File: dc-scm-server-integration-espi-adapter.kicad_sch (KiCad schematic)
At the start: 12 parts

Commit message: [#103753] Update symbol libraries
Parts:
- FD1001, FD1002, FD1003, FD1004, FD1007, FD1008: symbol Antmicro Symbols:Fiducial_1mm_Mask2mm -> antmicroFiducialMarks:Fiducial_1mm_Mask2mm
- H1001, H1002, H1003, H1004: symbol MechanicalParts:Spacer_Drill4.4mm_H6mm_9774060360R -> antmicroMechanicalParts:Spacer_Drill4.4mm_H6mm_9774060360R
- N1001: symbol Antmicro Symbols:antmicro_logo -> antmicroMechanicalParts:antmicro_logo
- N1002: symbol Antmicro Symbols:oshw_logo -> antmicroMechanicalParts:oshw_logo
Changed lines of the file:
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@@
 	)
 	(symbol
-		(lib_id "MechanicalParts:Spacer_Drill4.4mm_H6mm_9774060360R")
+		(lib_id "antmicroMechanicalParts:Spacer_Drill4.4mm_H6mm_9774060360R")
 		(at 224.79 134.62 0)
 		(unit 1)
@@
 	)
 	(symbol
-		(lib_id "Antmicro Symbols:Fiducial_1mm_Mask2mm")
+		(lib_id "antmicroFiducialMarks:Fiducial_1mm_Mask2mm")
 		(at 255.27 165.1 0)
 		(unit 1)
@@
 	)
 	(symbol
-		(lib_id "Antmicro Symbols:antmicro_logo")
+		(lib_id "antmicroMechanicalParts:antmicro_logo")
 		(at 224.79 166.37 0)
 		(unit 1)
@@
 	)
 	(symbol
-		(lib_id "MechanicalParts:Spacer_Drill4.4mm_H6mm_9774060360R")
+		(lib_id "antmicroMechanicalParts:Spacer_Drill4.4mm_H6mm_9774060360R")
 		(at 224.79 149.86 0)
 		(unit 1)
@@
 	)
 	(symbol
-		(lib_id "MechanicalParts:Spacer_Drill4.4mm_H6mm_9774060360R")
+		(lib_id "antmicroMechanicalParts:Spacer_Drill4.4mm_H6mm_9774060360R")
 		(at 224.79 142.24 0)
 		(unit 1)
@@
 	)
 	(symbol
-		(lib_id "Antmicro Symbols:oshw_logo")
+		(lib_id "antmicroMechanicalParts:oshw_logo")
 		(at 224.79 173.99 0)
 		(unit 1)
@@
 	)
 	(symbol
-		(lib_id "Antmicro Symbols:Fiducial_1mm_Mask2mm")
+		(lib_id "antmicroFiducialMarks:Fiducial_1mm_Mask2mm")
 		(at 255.27 142.24 0)
 		(unit 1)
@@
 	)
 	(symbol
-		(lib_id "Antmicro Symbols:GND")
+		(lib_id "antmicropower:GND")
 		(at 222.25 152.4 0)
 		(unit 1)
@@
 		(dnp no)
 		(fields_autoplaced yes)
-		(property "Reference" "#PWR01001"
+		(property "Reference" "#PWR1001"
 			(at 231.14 154.94 0)
 			(hide yes)
@@
 			(project "dc-scm-server-integration-espi-adapter"
 				(path "/df391740-647e-4ab6-9dcd-d61184d66fe9"
-					(reference "#PWR01001")
+					(reference "#PWR1001")
 					(unit 1)
 				)
@@
 	)
 	(symbol
-		(lib_id "Antmicro Symbols:Fiducial_1mm_Mask2mm")
+		(lib_id "antmicroFiducialMarks:Fiducial_1mm_Mask2mm")
 		(at 255.27 134.62 0)
 		(unit 1)
@@
 	)
 	(symbol
-		(lib_id "Antmicro Symbols:Fiducial_1mm_Mask2mm")
+		(lib_id "antmicroFiducialMarks:Fiducial_1mm_Mask2mm")
 		(at 255.27 172.72 0)
 		(unit 1)
@@
 	)
 	(symbol
-		(lib_id "Antmicro Symbols:Fiducial_1mm_Mask2mm")
+		(lib_id "antmicroFiducialMarks:Fiducial_1mm_Mask2mm")
 		(at 255.27 149.86 0)
 		(unit 1)
@@
 	)
 	(symbol
-		(lib_id "MechanicalParts:Spacer_Drill4.4mm_H6mm_9774060360R")
+		(lib_id "antmicroMechanicalParts:Spacer_Drill4.4mm_H6mm_9774060360R")
 		(at 224.79 127 0)
 		(unit 1)
@@
 	)
 	(symbol
-		(lib_id "Antmicro Symbols:Fiducial_1mm_Mask2mm")
+		(lib_id "antmicroFiducialMarks:Fiducial_1mm_Mask2mm")
 		(at 255.27 157.48 0)
 		(unit 1)

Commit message: [#103697] Reenumerate the entire schematic, rerouting eSPI to maintain bigger gap between traces, rerouting the LDO
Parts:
- renumbered FD1001 to FD1, FD1002 to FD2, FD1003 to FD3, FD1004 to FD4, FD1007 to FD5, FD1008 to FD6, H1001 to H1, H1002 to H2, H1003 to H3, H1004 to H4, N1001 to N1, N1002 to N2
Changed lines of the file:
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@@
 		(dnp no)
 		(fields_autoplaced yes)
-		(property "Reference" "H1002"
+		(property "Reference" "H2"
 			(at 233.68 133.35 0)
 			(show_name no)
@@
 			(project "dc-scm-server-integration-espi-adapter"
 				(path "/df391740-647e-4ab6-9dcd-d61184d66fe9"
-					(reference "H1002")
+					(reference "H2")
 					(unit 1)
 				)
@@
 		(dnp no)
 		(fields_autoplaced yes)
-		(property "Reference" "FD1007"
+		(property "Reference" "FD5"
 			(at 259.08 163.83 0)
 			(show_name no)
@@
 			(project "dc-scm-server-integration-espi-adapter"
 				(path "/df391740-647e-4ab6-9dcd-d61184d66fe9"
-					(reference "FD1007")
+					(reference "FD5")
 					(unit 1)
 				)
@@
 		(dnp no)
 		(fields_autoplaced yes)
-		(property "Reference" "N1001"
+		(property "Reference" "N1"
 			(at 231.14 164.3862 0)
 			(show_name no)
@@
 			(project "dc-scm-server-integration-espi-adapter"
 				(path "/df391740-647e-4ab6-9dcd-d61184d66fe9"
-					(reference "N1001")
+					(reference "N1")
 					(unit 1)
 				)
@@
 		(dnp no)
 		(fields_autoplaced yes)
-		(property "Reference" "H1004"
+		(property "Reference" "H4"
 			(at 233.68 148.59 0)
 			(show_name no)
@@
 			(project "dc-scm-server-integration-espi-adapter"
 				(path "/df391740-647e-4ab6-9dcd-d61184d66fe9"
-					(reference "H1004")
+					(reference "H4")
 					(unit 1)
 				)
@@
 		(dnp no)
 		(fields_autoplaced yes)
-		(property "Reference" "H1003"
+		(property "Reference" "H3"
 			(at 233.68 140.97 0)
 			(show_name no)
@@
 			(project "dc-scm-server-integration-espi-adapter"
 				(path "/df391740-647e-4ab6-9dcd-d61184d66fe9"
-					(reference "H1003")
+					(reference "H3")
 					(unit 1)
 				)
@@
 		(dnp no)
 		(fields_autoplaced yes)
-		(property "Reference" "N1002"
+		(property "Reference" "N2"
 			(at 231.14 172.0062 0)
 			(show_name no)
@@
 			(project "dc-scm-server-integration-espi-adapter"
 				(path "/df391740-647e-4ab6-9dcd-d61184d66fe9"
-					(reference "N1002")
+					(reference "N2")
 					(unit 1)
 				)
@@
 		(dnp no)
 		(fields_autoplaced yes)
-		(property "Reference" "FD1002"
+		(property "Reference" "FD2"
 			(at 259.08 140.97 0)
 			(show_name no)
@@
 			(project "dc-scm-server-integration-espi-adapter"
 				(path "/df391740-647e-4ab6-9dcd-d61184d66fe9"
-					(reference "FD1002")
+					(reference "FD2")
 					(unit 1)
 				)
@@
 		(dnp no)
 		(fields_autoplaced yes)
-		(property "Reference" "#PWR1001"
+		(property "Reference" "#PWR01"
 			(at 231.14 154.94 0)
 			(hide yes)
@@
 			(project "dc-scm-server-integration-espi-adapter"
 				(path "/df391740-647e-4ab6-9dcd-d61184d66fe9"
-					(reference "#PWR1001")
+					(reference "#PWR01")
 					(unit 1)
 				)
@@
 		(dnp no)
 		(fields_autoplaced yes)
-		(property "Reference" "FD1001"
+		(property "Reference" "FD1"
 			(at 259.08 133.35 0)
 			(show_name no)
@@
 			(project "dc-scm-server-integration-espi-adapter"
 				(path "/df391740-647e-4ab6-9dcd-d61184d66fe9"
-					(reference "FD1001")
+					(reference "FD1")
 					(unit 1)
 				)
@@
 		(dnp no)
 		(fields_autoplaced yes)
-		(property "Reference" "FD1008"
+		(property "Reference" "FD6"
 			(at 259.08 171.45 0)
 			(show_name no)
@@
 			(project "dc-scm-server-integration-espi-adapter"
 				(path "/df391740-647e-4ab6-9dcd-d61184d66fe9"
-					(reference "FD1008")
+					(reference "FD6")
 					(unit 1)
 				)
@@
 		(dnp no)
 		(fields_autoplaced yes)
-		(property "Reference" "FD1003"
+		(property "Reference" "FD3"
 			(at 259.08 148.59 0)
 			(show_name no)
@@
 			(project "dc-scm-server-integration-espi-adapter"
 				(path "/df391740-647e-4ab6-9dcd-d61184d66fe9"
-					(reference "FD1003")
+					(reference "FD3")
 					(unit 1)
 				)
@@
 		(dnp no)
 		(fields_autoplaced yes)
-		(property "Reference" "H1001"
+		(property "Reference" "H1"
 			(at 233.68 125.73 0)
 			(show_name no)
@@
 			(project "dc-scm-server-integration-espi-adapter"
 				(path "/df391740-647e-4ab6-9dcd-d61184d66fe9"
-					(reference "H1001")
+					(reference "H1")
 					(unit 1)
 				)
@@
 		(dnp no)
 		(fields_autoplaced yes)
-		(property "Reference" "FD1004"
+		(property "Reference" "FD4"
 			(at 259.08 156.21 0)
 			(show_name no)
@@
 			(project "dc-scm-server-integration-espi-adapter"
 				(path "/df391740-647e-4ab6-9dcd-d61184d66fe9"
-					(reference "FD1004")
+					(reference "FD4")
 					(unit 1)
 				)

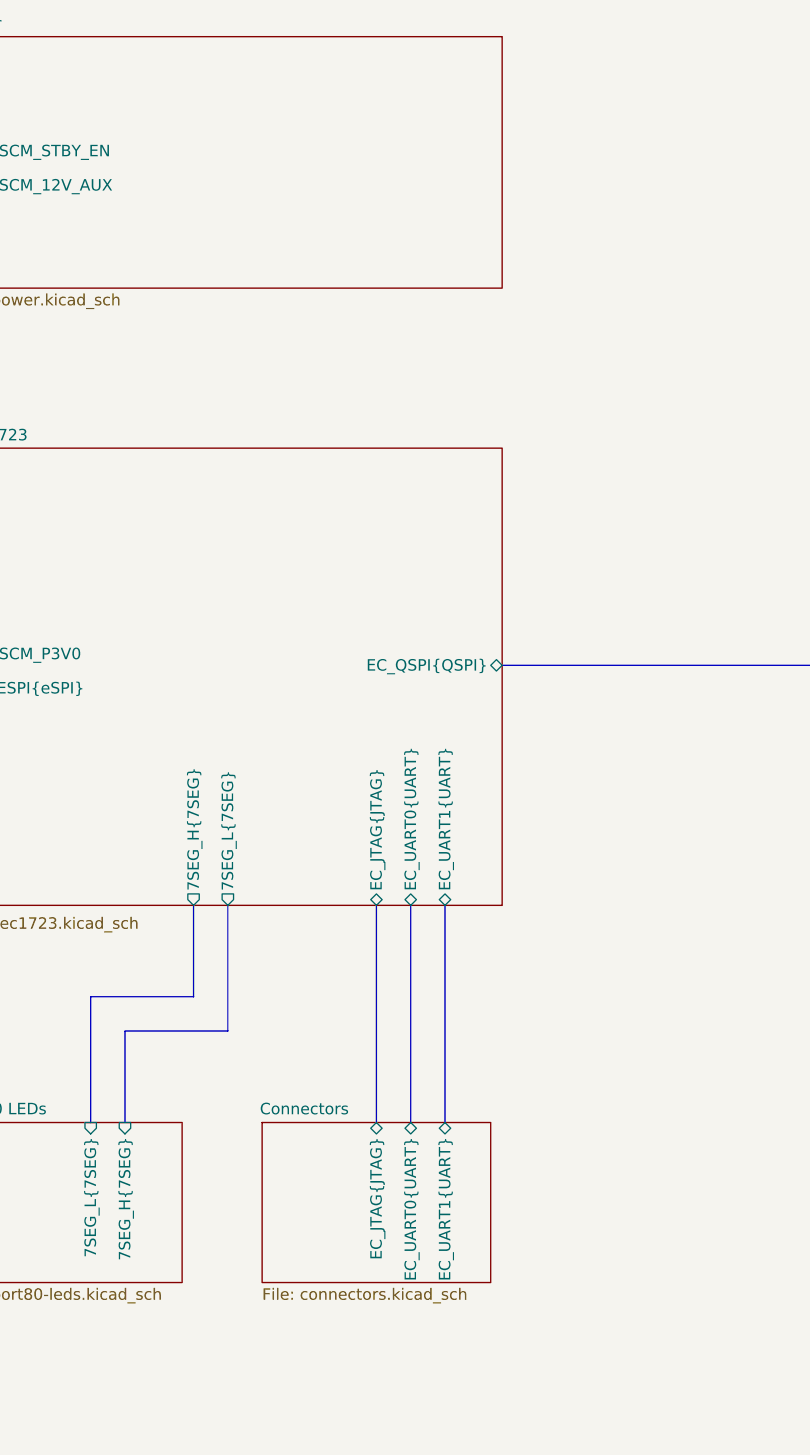
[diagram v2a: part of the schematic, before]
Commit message: [#103697] Change LDO layout, add power from USB, fix length tuning, change In4.Cu to GND/SIG and In5.Cu to 3V3, cleanup the design
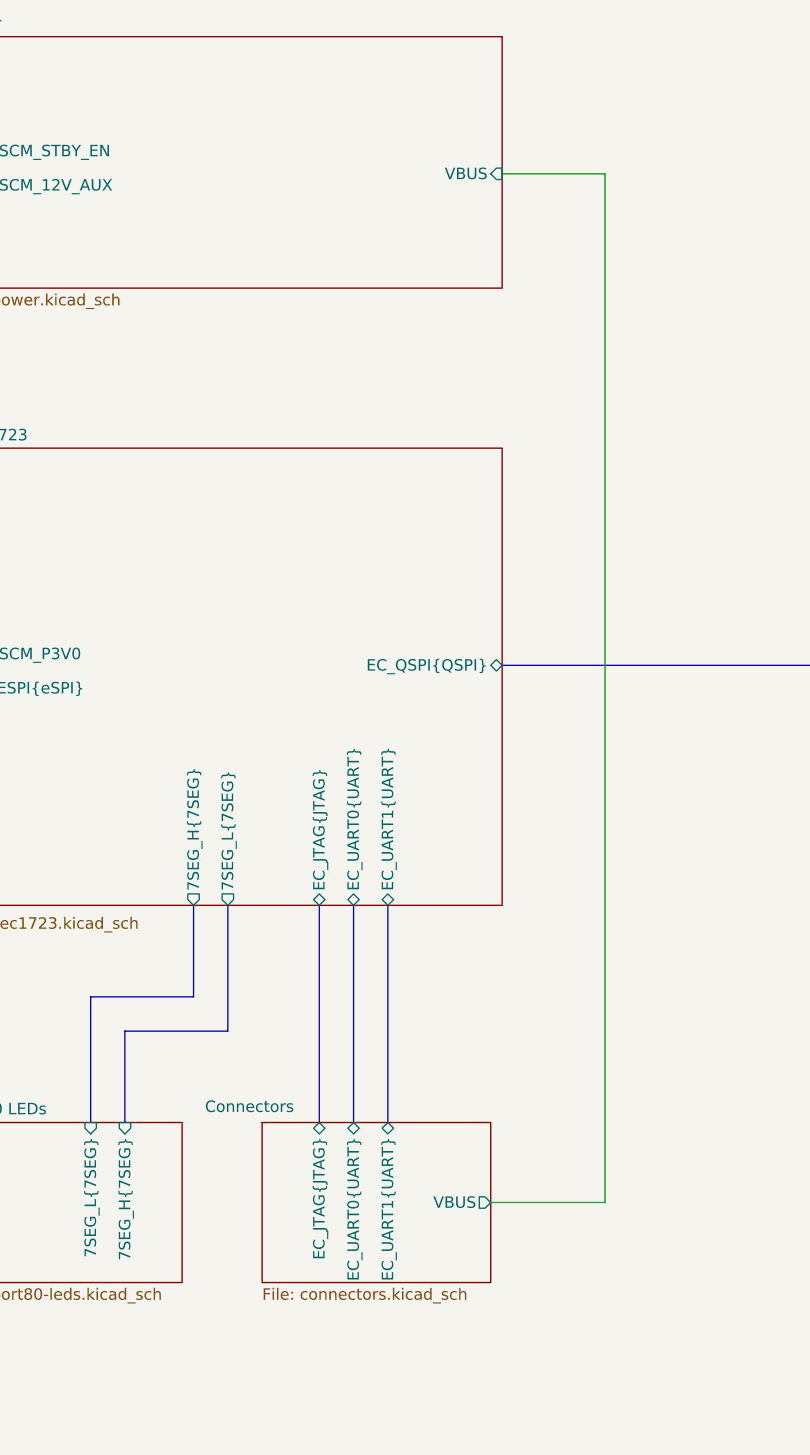
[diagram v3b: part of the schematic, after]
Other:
- sheet Connectors ports: added VBUS; removed none
- sheet Power ports: added VBUS; removed none
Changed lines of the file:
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@@
 		(color 0 0 0 0)
 	)
+	(wire
+		(pts
+			(xy 190.5 35.56) (xy 179.07 35.56)
+		)
+		(stroke
+			(width 0)
+			(type default)
+		)
+	)
 	(bus
 		(pts
@@
 	(bus
 		(pts
-			(xy 165.1 116.84) (xy 165.1 140.97)
+			(xy 158.75 116.84) (xy 158.75 140.97)
 		)
 		(stroke
@@
 	(bus
 		(pts
-			(xy 168.91 116.84) (xy 168.91 140.97)
+			(xy 162.56 116.84) (xy 162.56 140.97)
 		)
 		(stroke
@@
 	(wire
 		(pts
+			(xy 190.5 149.86) (xy 190.5 35.56)
+		)
+		(stroke
+			(width 0)
+			(type default)
+		)
+	)
+	(wire
+		(pts
 			(xy 69.85 88.9) (xy 118.11 88.9)
 		)
@@
 		)
 	)
+	(wire
+		(pts
+			(xy 177.8 149.86) (xy 190.5 149.86)
+		)
+		(stroke
+			(width 0)
+			(type default)
+		)
+	)
 	(bus
 		(pts
@@
 	(bus
 		(pts
-			(xy 172.72 116.84) (xy 172.72 140.97)
+			(xy 166.37 116.84) (xy 166.37 140.97)
 		)
 		(stroke
@@
 			)
 		)
+		(pin "VBUS" input
+			(at 179.07 35.56 0)
+			(effects
+				(font
+					(size 1.27 1.27)
+				)
+				(justify right)
+			)
+		)
 		(instances
 			(project "dc-scm-server-integration-espi-adapter"
@@
 		)
 		(property "Sheetname" "Connectors"
-			(at 152.146 140.208 0)
+			(at 146.05 139.954 0)
 			(show_name no)
 			(do_not_autoplace no)
@@
 		)
 		(pin "EC_JTAG{JTAG}" bidirectional
-			(at 165.1 140.97 90)
+			(at 158.75 140.97 90)
 			(effects
 				(font
@@
 		)
 		(pin "EC_UART0{UART}" bidirectional
-			(at 168.91 140.97 90)
+			(at 162.56 140.97 90)
 			(effects
 				(font
@@
 		)
 		(pin "EC_UART1{UART}" bidirectional
-			(at 172.72 140.97 90)
+			(at 166.37 140.97 90)
+			(effects
+				(font
+					(size 1.27 1.27)
+				)
+				(justify right)
+			)
+		)
+		(pin "VBUS" output
+			(at 177.8 149.86 0)
 			(effects
 				(font
@@
 		)
 		(pin "EC_JTAG{JTAG}" bidirectional
-			(at 165.1 116.84 270)
+			(at 158.75 116.84 270)
 			(effects
 				(font
@@
 		)
 		(pin "EC_UART0{UART}" bidirectional
-			(at 168.91 116.84 270)
+			(at 162.56 116.84 270)
 			(effects
 				(font
@@
 		)
 		(pin "EC_UART1{UART}" bidirectional
-			(at 172.72 116.84 270)
-			(effects
-				(font
+			(at 166.37 116.84 270)
+			(effects
+				(font
